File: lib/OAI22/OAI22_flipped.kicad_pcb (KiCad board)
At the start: 2 copper layers, 8 parts

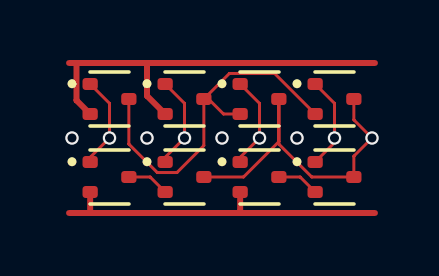
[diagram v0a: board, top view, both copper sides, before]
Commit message: High-density layout with pitch of 1.1mm, which gains 23% !!
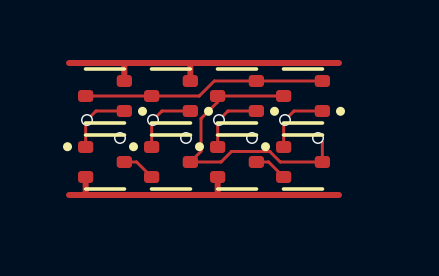
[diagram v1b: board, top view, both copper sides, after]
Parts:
- moved P4 1.16 mm to (7.70, 3.30)
- moved N4 1.05 mm to (7.70, 1.10), turned to 180 degrees
- moved P3 0.90 mm to (5.50, 3.30)
- moved N3 0.76 mm to (5.50, 1.10), turned to 180 degrees
- moved P2 0.67 mm to (3.30, 3.30)
- moved P1 0.52 mm to (1.10, 3.30)
- moved N2 0.46 mm to (3.30, 1.10), turned to 180 degrees
- moved N1 0.18 mm to (1.10, 1.10), turned to 180 degrees
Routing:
- net intN: track 12.4 -> 8.10 mm
- net GND: track 14.1 -> 10.2 mm
- net Y: track 12.0 -> 10.3 mm
- net VDD: track 11.6 -> 10.3 mm
- net B1: track 3.13 -> 2.29 mm
- net A2: track 3.13 -> 2.29 mm
- net A1: track 3.13 -> 2.29 mm
- net B2: track 3.13 -> 2.29 mm
- net (no net): vias 4 -> 3

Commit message: All cells now use 1mm*4mm grid rather than 1.1mm*4.4mm
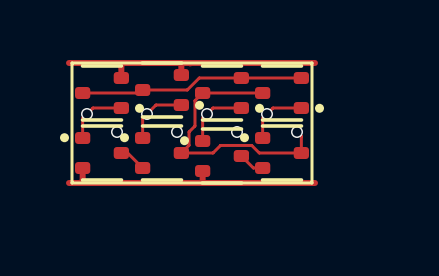
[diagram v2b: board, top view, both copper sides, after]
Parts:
- moved P4 0.76 mm to (7.00, 3.00)
- moved N4 0.71 mm to (7.00, 1.00)
- moved P3 0.54 mm to (5.00, 3.10)
- moved N3 0.51 mm to (5.00, 1.00)
- moved P2 0.42 mm to (3.00, 3.00)
- moved N2 0.36 mm to (3.00, 0.90)
- moved P1 0.32 mm to (1.00, 3.00)
- moved N1 0.14 mm to (1.00, 1.00)
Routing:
- net VDD: track 10.3 -> 9.16 mm
- net Y: track 10.3 -> 9.26 mm
- net GND: track 10.2 -> 9.17 mm
- net intN: track 8.10 -> 7.50 mm

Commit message: Make the pads of my SOT523 footprint very slightly smaller, which is enough to route all the cells and leave the mosfets exactly on the grid
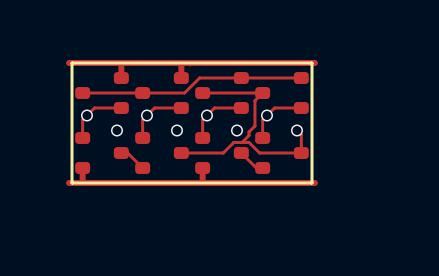
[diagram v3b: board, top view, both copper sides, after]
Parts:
- N1, N2, N3, N4, P1, P2, P3, P4: footprint Package_TO_SOT_SMD:SOT-523 -> RV523:SOT523
- moved P3 0.10 mm to (5.00, 3.00)
- moved N2 0.10 mm to (3.00, 1.00)

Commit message: Propagate MOSFET values to the cells' PCBs
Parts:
- N1, N2, N3, N4: value (none) -> NMOS
- P1, P2, P3, P4: value (none) -> PMOS
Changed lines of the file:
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@@
 			)
 		)
-		(property "Value" ""
+		(property "Value" "NMOS"
 			(at 0 0 180)
 			(layer "F.Fab")
@@
 			)
 		)
-		(property "Value" ""
+		(property "Value" "PMOS"
 			(at 0 0 0)
 			(layer "F.Fab")
@@
 			)
 		)
-		(property "Value" ""
+		(property "Value" "PMOS"
 			(at 0 0 0)
 			(layer "F.Fab")
@@
 			)
 		)
-		(property "Value" ""
+		(property "Value" "PMOS"
 			(at 0 0 0)
 			(layer "F.Fab")
@@
 			)
 		)
-		(property "Value" ""
+		(property "Value" "PMOS"
 			(at 0 0 0)
 			(layer "F.Fab")
@@
 			)
 		)
-		(property "Value" ""
+		(property "Value" "NMOS"
 			(at 0 0 180)
 			(layer "F.Fab")
@@
 			)
 		)
-		(property "Value" ""
+		(property "Value" "NMOS"
 			(at 0 0 180)
 			(layer "F.Fab")
@@
 			)
 		)
-		(property "Value" ""
+		(property "Value" "NMOS"
 			(at 0 0 180)
 			(layer "F.Fab")
